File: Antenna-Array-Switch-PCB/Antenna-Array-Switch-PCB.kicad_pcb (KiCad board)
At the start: 4 copper layers, 98 x 98 mm, 172 parts, among them J1 Conn_Coaxial, J10 Conn_Coaxial, J11 Conn_Coaxial, J12 RFShield_OnePiece, J2 Conn_Coaxial, J3 Conn_Coaxial, J4 Conn_SMA, J5 Conn_SMA, J6 Conn_SMA, J7 Conn_Coaxial, J8 Conn_Coaxial, J9 Conn_Coaxial, SW1 TS-1187A-B-A-B, SW2 TS-1187A-B-A-B, U1 PGA-103, U10 TPS22917DBV, U11 PGA-103, U12 TPS22917DBV, U13 PGA-103, U14 TPS22917DBV, U15 PGA-103, U16 TPS22917DBV, U17 PGA-103, U18 TPS22917DBV, U19 PGA-103, U2 TPS22917DBV, U3 TPS22917DBV, U4 PGA-103, U5 TPS22917DBV, U6 PGA-103, U7 SKY13418-485LF, U8 LM1117IMP-3.3, U9 RP2040-Zero

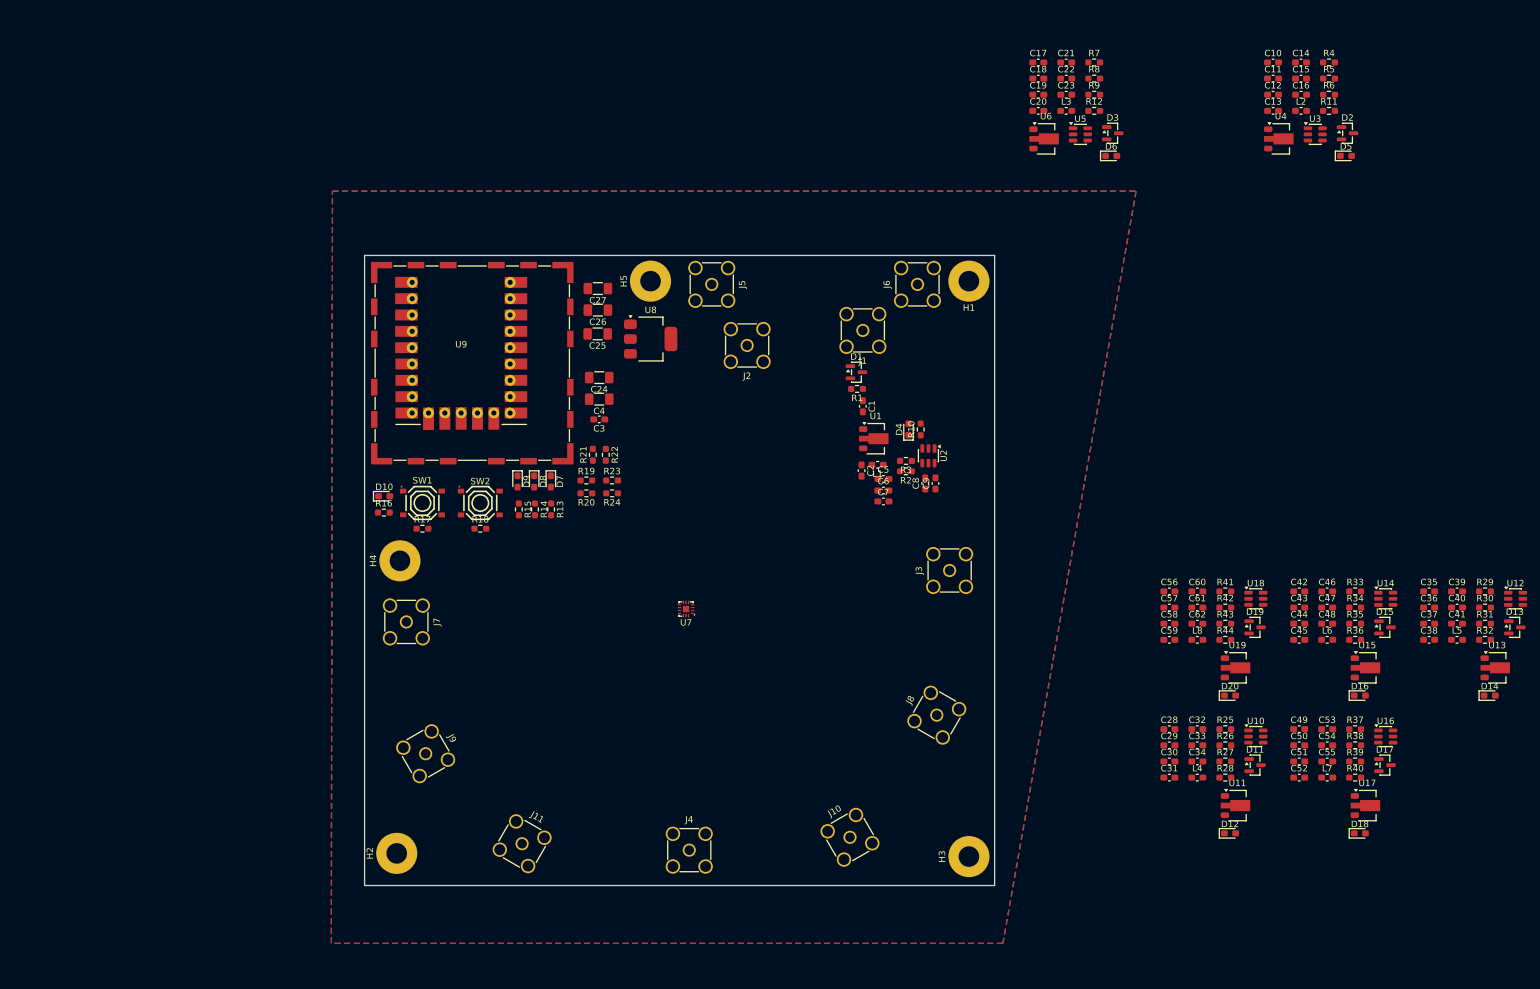
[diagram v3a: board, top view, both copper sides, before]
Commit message: PCB: Replicate layouts to all LNA chains
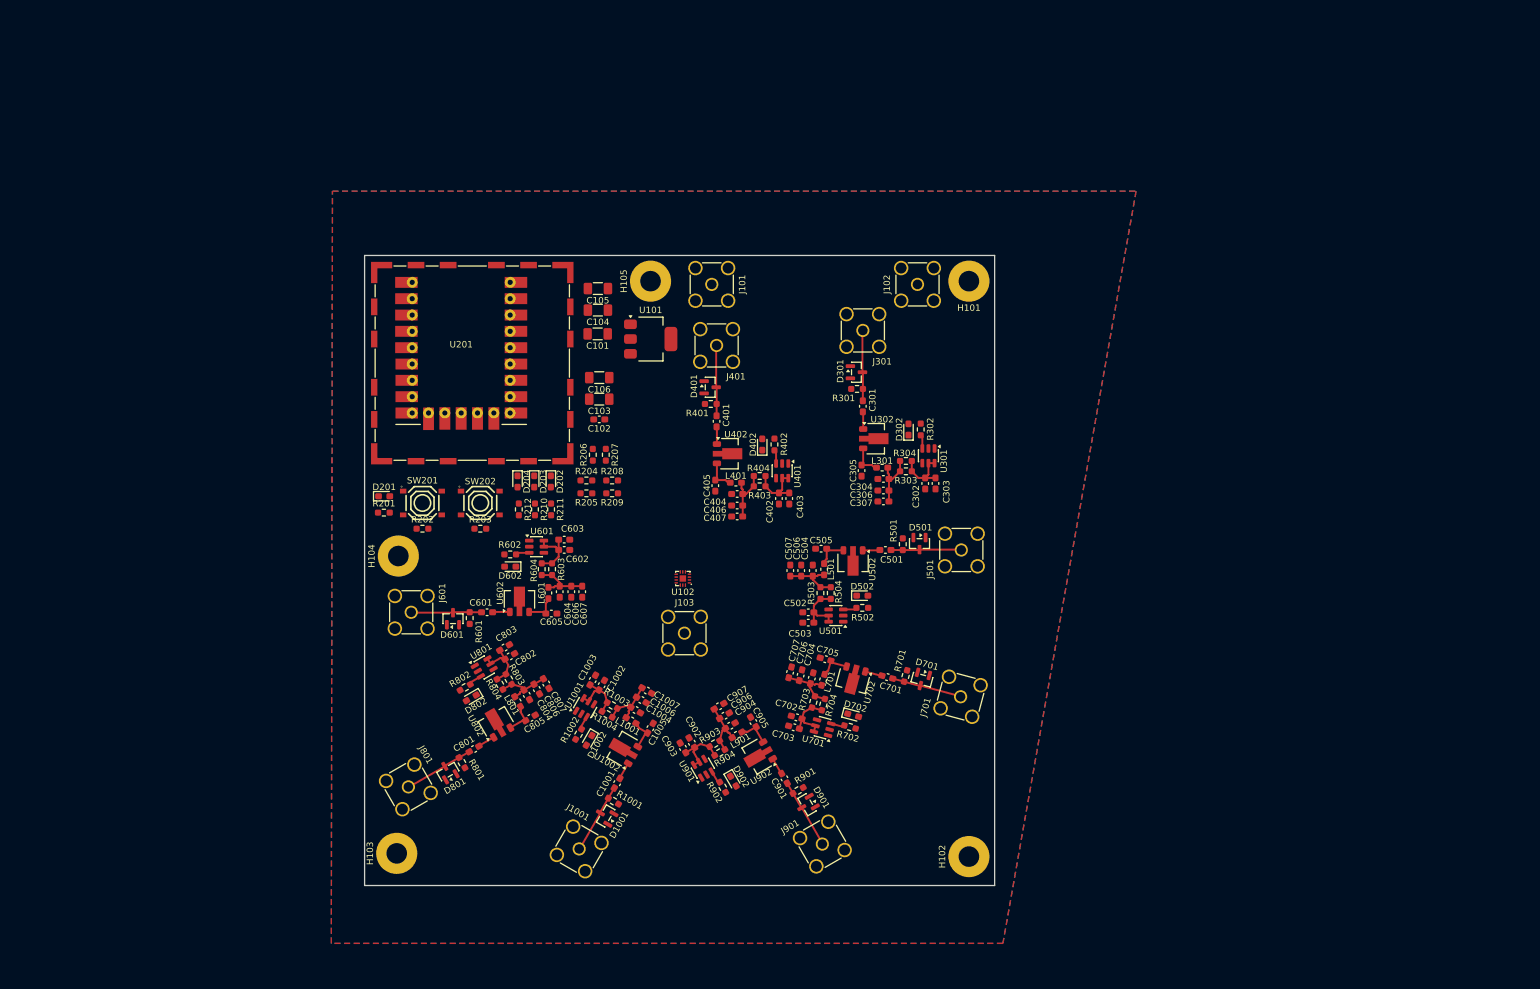
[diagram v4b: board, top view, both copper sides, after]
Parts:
- moved D801 147.5 mm to (112.9, 130.3), turned to 120 degrees
- moved R801 141.5 mm to (115.1, 128.9), turned to -60 degrees
- moved U801 140.6 mm to (118.6, 114.1), turned to 30 degrees
- moved R802 139.0 mm to (115.7, 117.2), turned to -150 degrees
- moved D802 138.2 mm to (116.6, 118.8), turned to -150 degrees
- moved U802 135.8 mm to (120.4, 122.5), turned to 120 degrees
- moved R804 133.2 mm to (121.0, 116.7), turned to -60 degrees
- moved R803 131.9 mm to (122.4, 115.9), turned to -60 degrees
- moved C801 130.7 mm to (117.0, 126.8), turned to 30 degrees
- moved D601 126.8 mm to (113.8, 106.5), turned to 90 degrees
- moved L801 126.3 mm to (123.8, 119.4), turned to -60 degrees
- moved C805 125.5 mm to (125.8, 121.9), turned to 30 degrees
- moved C803 123.7 mm to (121.8, 111.0), turned to -150 degrees
- moved C806 123.6 mm to (126.8, 117.4), turned to 120 degrees
- moved C802 123.0 mm to (122.6, 112.4), turned to -150 degrees
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- renumbered C56 to C1001, C57 to C1002, C58 to C1003, C59 to C1004, C60 to C1005, C61 to C1006, C62 to C1007, C25 to C101, C3 to C102, C4 to C103, C26 to C104, C27 to C105, C24 to C106, C1 to C301, C8 to C302, C9 to C303, C5 to C304, C2 to C305, C6 to C306, C7 to C307, C10 to C401, C11 to C402, C12 to C403, C13 to C404, C14 to C405, C15 to C406, C16 to C407, C17 to C501, C18 to C502, C19 to C503, C20 to C504, C21 to C505, C22 to C506, C23 to C507, C28 to C601, C29 to C602, C30 to C603, C31 to C604, C32 to C605, C33 to C606, C34 to C607, C35 to C701, C36 to C702, C37 to C703, C38 to C704, C39 to C705, C40 to C706, C41 to C707, C42 to C801, C43 to C802, C44 to C803, C45 to C804, C46 to C805, C47 to C806, C48 to C807, C49 to C901, C50 to C902, C51 to C903, C52 to C904, C53 to C905, C54 to C906, C55 to C907, D19 to D1001, D20 to D1002, D10 to D201, D7 to D202, D8 to D203, D9 to D204, D1 to D301, D4 to D302, D2 to D401, D5 to D402, D3 to D501, D6 to D502, D11 to D601, D12 to D602, D13 to D701, D14 to D702, D15 to D801, D16 to D802, D17 to D901, D18 to D902, H1 to H101, H3 to H102, H2 to H103, H4 to H104, H5 to H105, J11 to J1001, J5 to J101, J6 to J102, J4 to J103, J12 to J201, J1 to J301, J2 to J401, J3 to J501, J7 to J601, J8 to J701, J9 to J801, J10 to J901, L8 to L1001, L1 to L301, L2 to L401, L3 to L501, L4 to L601, L5 to L701, L6 to L801, L7 to L901, R41 to R1001, R42 to R1002, R43 to R1003, R44 to R1004, R16 to R201, R17 to R202, R18 to R203, R19 to R204, R20 to R205, R21 to R206, R22 to R207, R23 to R208, R24 to R209, R14 to R210, R13 to R211, R15 to R212, R1 to R301, R10 to R302, R2 to R303, R3 to R304, R4 to R401, R11 to R402, R5 to R403, R6 to R404, R7 to R501, R12 to R502, R8 to R503, R9 to R504, R25 to R601, R26 to R602, R27 to R603, R28 to R604, R29 to R701, R30 to R702, R31 to R703, R32 to R704, R33 to R801, R34 to R802, R35 to R803, R36 to R804, R37 to R901, R38 to R902, R39 to R903, R40 to R904, SW1 to SW201, SW2 to SW202, U18 to U1001, U19 to U1002, U8 to U101, U7 to U102, U9 to U201, U2 to U301, U1 to U302, U3 to U401, U4 to U402, U5 to U501, U6 to U502, U10 to U601, U11 to U602, U12 to U701, U13 to U702, U14 to U801, U15 to U802, U16 to U901, U17 to U902
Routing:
- net Net-(J701-In): track 0.00 -> 11.0 mm
- net Net-(J601-In): track 0.00 -> 11.0 mm
- net Net-(J501-In): track 0.00 -> 11.0 mm
- net Net-(J401-In): track 0.00 -> 11.0 mm
- net Net-(J301-In): track 0.00 -> 11.0 mm
- net Net-(J801-In): track 0.00 -> 11.0 mm
- net Net-(J901-In): track 0.00 -> 11.0 mm
- net Net-(J1001-In): track 0.00 -> 11.0 mm
- net Net-(U701-QOD): track 0.00 -> 9.18 mm
- net Net-(U401-QOD): track 0.00 -> 9.18 mm
- net Net-(U301-QOD): track 0.00 -> 9.18 mm
- net Net-(U501-QOD): track 0.00 -> 9.18 mm
- net Net-(U601-QOD): track 0.00 -> 9.18 mm
- net Net-(U901-QOD): track 0.00 -> 9.18 mm
- net Net-(U801-QOD): track 0.00 -> 9.18 mm
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
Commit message: PCB Sch: Add filters at control lines
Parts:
- added C1008: 100pF, Capacitor_SMD:C_0603_1608Metric_Pad1.08x0.95mm_HandSolder, F.Cu at (128.4, 14.7)
- added C107: 100pF, Capacitor_SMD:C_0603_1608Metric_Pad1.08x0.95mm_HandSolder, F.Cu at (143.2, 90.5)
- added C108: 100pF, Capacitor_SMD:C_0603_1608Metric_Pad1.08x0.95mm_HandSolder, F.Cu at (135.5, 77.2)
- added C109: 100pF, Capacitor_SMD:C_0603_1608Metric_Pad1.08x0.95mm_HandSolder, F.Cu at (137.8, 90.8)
- added C308: 100pF, Capacitor_SMD:C_0603_1608Metric_Pad1.08x0.95mm_HandSolder, F.Cu at (187.8, 75.8)
- added C408: 100pF, Capacitor_SMD:C_0603_1608Metric_Pad1.08x0.95mm_HandSolder, F.Cu at (134.8, 21.8)
- added C508: 100pF, Capacitor_SMD:C_0603_1608Metric_Pad1.08x0.95mm_HandSolder, F.Cu at (141.1, 14.7)
- added C608: 100pF, Capacitor_SMD:C_0603_1608Metric_Pad1.08x0.95mm_HandSolder, F.Cu at (134.8, 14.7)
- added C708: 100pF, Capacitor_SMD:C_0603_1608Metric_Pad1.08x0.95mm_HandSolder, F.Cu at (141.1, 21.8)
- added C808: 100pF, Capacitor_SMD:C_0603_1608Metric_Pad1.08x0.95mm_HandSolder, F.Cu at (128.4, 21.8)
- added C908: 100pF, Capacitor_SMD:C_0603_1608Metric_Pad1.08x0.95mm_HandSolder, F.Cu at (134.8, 28.8)
- added R1005: 1k, Resistor_SMD:R_0603_1608Metric_Pad0.98x0.95mm_HandSolder, F.Cu at (128.4, 17.2)
- added R101: 1k, Resistor_SMD:R_0603_1608Metric_Pad0.98x0.95mm_HandSolder, F.Cu at (140.5, 90.5)
- added R102: 1k, Resistor_SMD:R_0603_1608Metric_Pad0.98x0.95mm_HandSolder, F.Cu at (138.0, 77.2)
- added R103: 1k, Resistor_SMD:R_0603_1608Metric_Pad0.98x0.95mm_HandSolder, F.Cu at (135.0, 90.8)
- added R305: 1k, Resistor_SMD:R_0603_1608Metric_Pad0.98x0.95mm_HandSolder, F.Cu at (187.8, 74.0)
- added R405: 1k, Resistor_SMD:R_0603_1608Metric_Pad0.98x0.95mm_HandSolder, F.Cu at (134.8, 24.3)
- added R505: 1k, Resistor_SMD:R_0603_1608Metric_Pad0.98x0.95mm_HandSolder, F.Cu at (141.1, 17.2)
- added R605: 1k, Resistor_SMD:R_0603_1608Metric_Pad0.98x0.95mm_HandSolder, F.Cu at (134.8, 17.2)
- added R705: 1k, Resistor_SMD:R_0603_1608Metric_Pad0.98x0.95mm_HandSolder, F.Cu at (141.1, 24.3)
- added R805: 1k, Resistor_SMD:R_0603_1608Metric_Pad0.98x0.95mm_HandSolder, F.Cu at (128.4, 24.3)
- added R905: 1k, Resistor_SMD:R_0603_1608Metric_Pad0.98x0.95mm_HandSolder, F.Cu at (134.8, 31.3)
- moved C102 16.9 mm to (136.4, 58.6)
- moved C106 16.9 mm to (136.4, 52.1)
- moved C103 16.9 mm to (136.4, 55.5)
- moved C105 13.5 mm to (136.8, 68.7)
- moved C104 13.5 mm to (136.8, 72.0)
- moved C101 11.1 mm to (147.2, 63.6), turned to -90 degrees
- moved R301 4.43 mm to (180.2, 68.2), turned to 0 degrees
- moved U101 3.78 mm to (140.8, 63.5), turned to 180 degrees
- moved C302 2.26 mm to (186.9, 83.2)
- moved C303 2.26 mm to (188.6, 83.2)
- moved C304 2.26 mm to (180.4, 82.5)
- moved C305 2.26 mm to (177.1, 81.2)
- moved C306 2.26 mm to (180.4, 84.3)
- moved C307 2.26 mm to (180.4, 86.0)
- moved L301 2.26 mm to (180.2, 80.8)
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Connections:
- R1002 pad 1: LNA_ENABLE_7 -> Net-(U1001-ON)
- R302 pad 1: LNA_ENABLE_0 -> Net-(U301-ON)
- R402 pad 1: LNA_ENABLE_1 -> Net-(U401-ON)
- R502 pad 1: LNA_ENABLE_2 -> Net-(U501-ON)
- R602 pad 1: LNA_ENABLE_3 -> Net-(U601-ON)
- R702 pad 1: LNA_ENABLE_4 -> Net-(U701-ON)
- R802 pad 1: LNA_ENABLE_5 -> Net-(U801-ON)
- R902 pad 1: LNA_ENABLE_6 -> Net-(U901-ON)
- U1001 pad 3: LNA_ENABLE_7 -> Net-(U1001-ON)
- U102 pad 5: SWITCH_CTRL3_AT_1V8 -> Net-(U102-CTRL3)
- U102 pad 6: SWITCH_CTRL2_AT_1V8 -> Net-(U102-CTRL2)
- U102 pad 7: SWITCH_CTRL1_AT_1V8 -> Net-(U102-CTRL1)
- U301 pad 3: LNA_ENABLE_0 -> Net-(U301-ON)
- U401 pad 3: LNA_ENABLE_1 -> Net-(U401-ON)
- U501 pad 3: LNA_ENABLE_2 -> Net-(U501-ON)
- U601 pad 3: LNA_ENABLE_3 -> Net-(U601-ON)
- U701 pad 3: LNA_ENABLE_4 -> Net-(U701-ON)
- U801 pad 3: LNA_ENABLE_5 -> Net-(U801-ON)
- U901 pad 3: LNA_ENABLE_6 -> Net-(U901-ON)
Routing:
- net +3.3V: track 0.00 -> 60.9 mm, vias 0 -> 8
- net /AntennaBranch/LNA_RF_OUTPUT: track 0.00 -> 32.7 mm
- net /AntennaBranch5/LNA_RF_OUTPUT: track 0.00 -> 30.5 mm
- net +5V: track 0.00 -> 28.7 mm, vias 0 -> 17
- net Net-(U102-CTRL2): track 0.00 -> 28.5 mm, vias 0 -> 2
- net /AntennaBranch4/LNA_RF_OUTPUT: track 0.00 -> 27.2 mm
- net /AntennaBranch6/LNA_RF_OUTPUT: track 0.00 -> 26.8 mm
- net /AntennaBranch7/LNA_RF_OUTPUT: track 0.00 -> 25.7 mm
- net /AntennaBranch2/LNA_RF_OUTPUT: track 0.00 -> 21.6 mm
- net /AntennaBranch3/LNA_RF_OUTPUT: track 0.00 -> 20.8 mm
- net Net-(U102-CTRL1): track 0.00 -> 17.9 mm, vias 0 -> 2
- net /AntennaBranch1/LNA_RF_OUTPUT: track 0.00 -> 17.7 mm
- net Net-(U102-CTRL3): track 0.00 -> 13.9 mm, vias 0 -> 2
- net SWITCH_CTRL3_AT_1V8: track 0.00 -> 7.81 mm
- net SWITCH_CTRL1_AT_1V8: track 0.00 -> 7.79 mm
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- added copper zone on In2.Cu, net +5V

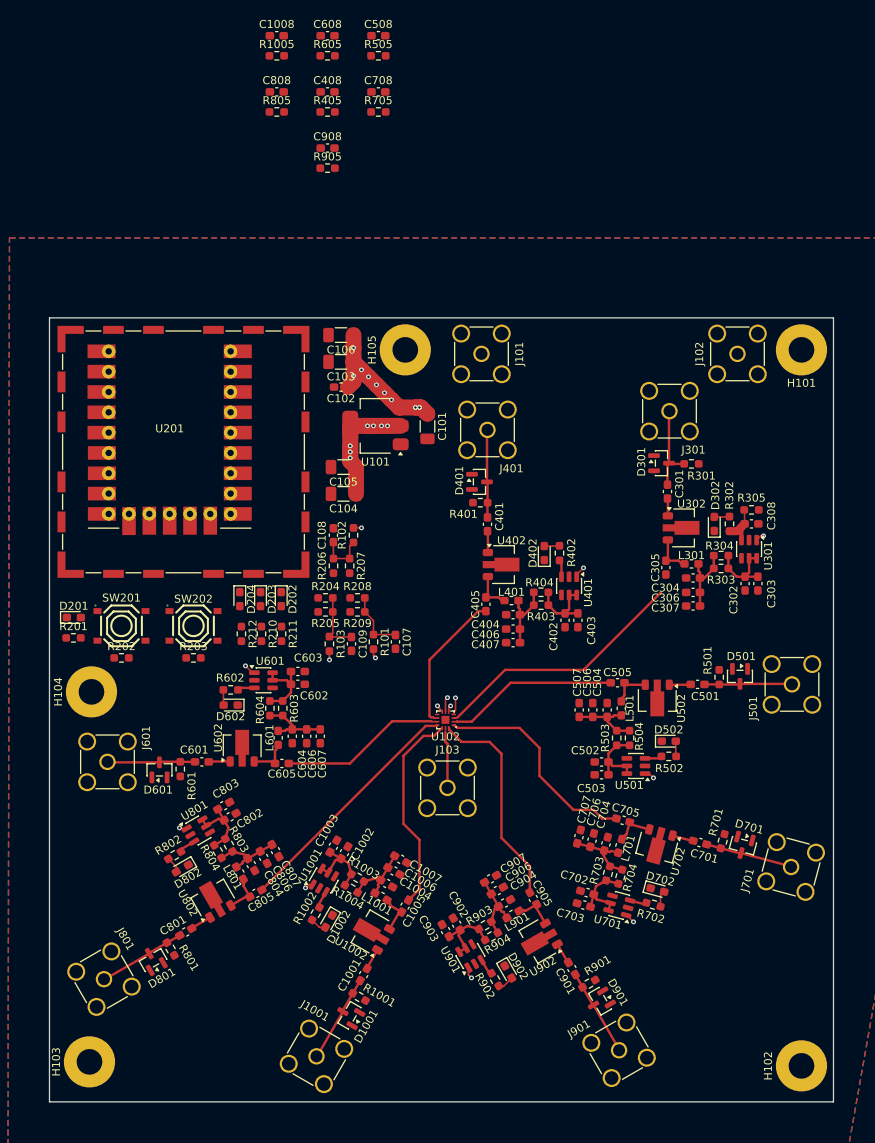
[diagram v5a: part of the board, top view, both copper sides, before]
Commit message: PCB: More layout, legends
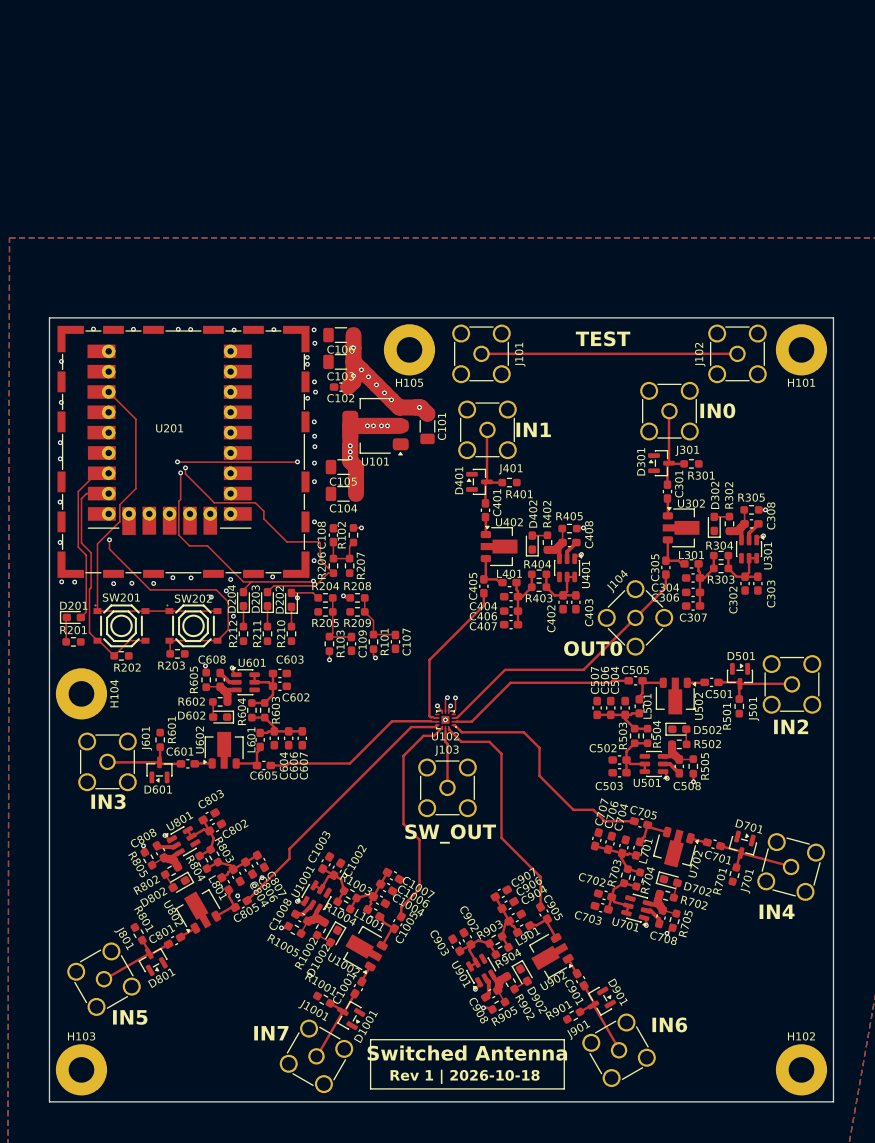
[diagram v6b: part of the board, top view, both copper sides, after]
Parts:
- added J104: Conn_Coaxial, Connector_Coaxial:SMA_Amphenol_901-144_Vertical, F.Cu at (173.2, 87.5)
- moved C1008 110.3 mm to (131.5, 125.0), turned to -30 degrees
- moved R1005 109.3 mm to (130.7, 126.5), turned to -30 degrees
- moved C708 109.0 mm to (176.4, 124.9), turned to 75 degrees
- moved C908 107.7 mm to (155.3, 134.5), turned to 30 degrees
- moved R705 107.7 mm to (178.1, 125.3), turned to 75 degrees
- moved R905 106.9 mm to (156.2, 136.0), turned to 30 degrees
- moved C508 98.8 mm to (178.7, 106.1), turned to 90 degrees
- moved R505 97.2 mm to (180.5, 106.1), turned to 90 degrees
- moved C808 96.1 mm to (113.9, 116.7), turned to -60 degrees
- moved R805 94.7 mm to (112.4, 117.6), turned to -60 degrees
- moved C608 81.6 mm to (121.3, 95.2), turned to -90 degrees
- moved R605 79.5 mm to (119.6, 95.2), turned to -90 degrees
- moved C408 63.9 mm to (165.0, 78.1), turned to 180 degrees
- moved R405 60.2 mm to (165.0, 76.3), turned to 180 degrees
- moved R1001 4.43 mm to (134.3, 135.2), turned to 150 degrees
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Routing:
- net LNA_ENABLE_4: track 0.00 -> 110.4 mm, vias 0 -> 1
- net LNA_ENABLE_2: track 0.00 -> 109.0 mm, vias 0 -> 1
- net LNA_ENABLE_6: track 0.00 -> 85.9 mm, vias 0 -> 1
- net LNA_ENABLE_0: track 0.00 -> 75.9 mm, vias 0 -> 1
- net LNA_ENABLE_7: track 0.00 -> 62.5 mm, vias 0 -> 1
- net LNA_ENABLE_5: track 0.00 -> 54.5 mm, vias 0 -> 1
- net LNA_ENABLE_1: track 0.00 -> 53.1 mm, vias 0 -> 1
- net SWITCH_CTRL3_AT_3V3: track 0.00 -> 49.6 mm, vias 0 -> 3
- net SWITCH_CTRL2_AT_3V3: track 0.00 -> 47.5 mm, vias 0 -> 1
- net MCU_3V3: track 0.00 -> 45.8 mm
- net SWITCH_CTRL1_AT_3V3: track 0.00 -> 45.7 mm, vias 0 -> 3
- net LNA_ENABLE_3: track 0.00 -> 42.0 mm, vias 0 -> 1
- net GP_BUTTON_2: track 0.00 -> 35.1 mm, vias 0 -> 1
- net Net-(J101-In): track 0.00 -> 32.0 mm
- net GP_BUTTON_1: track 0.00 -> 29.1 mm
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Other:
- board text added: "IN0"
- board text added: "IN1"
- board text added: "IN2"
- board text added: "IN3"
- board text added: "IN4"
- board text added: "IN5"
- board text added: "IN6"
- board text added: "IN7"
- board text added: "OUT0"
- board text added: "Rev 1 | 2026-10-18"
- board text added: "SW_OUT"
- board text added: "Switched Antenna"
- board text added: "TEST"
